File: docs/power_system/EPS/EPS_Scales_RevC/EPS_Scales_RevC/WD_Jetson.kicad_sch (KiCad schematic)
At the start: 40 parts, among them J3 Conn_01x04, J4 Conn_01x04, U5 TLV1704

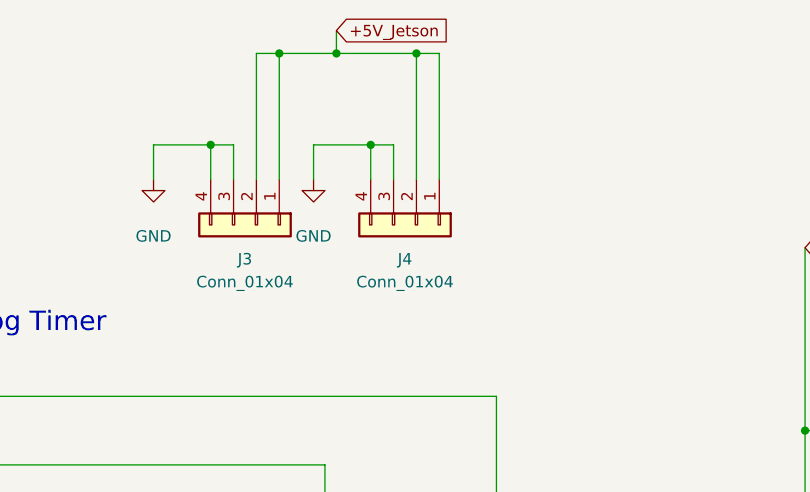
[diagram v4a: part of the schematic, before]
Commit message: WIP EPS REV C.
Removed XNOR implementation, redid layout for compactness, restarting routing for more efficient traces.
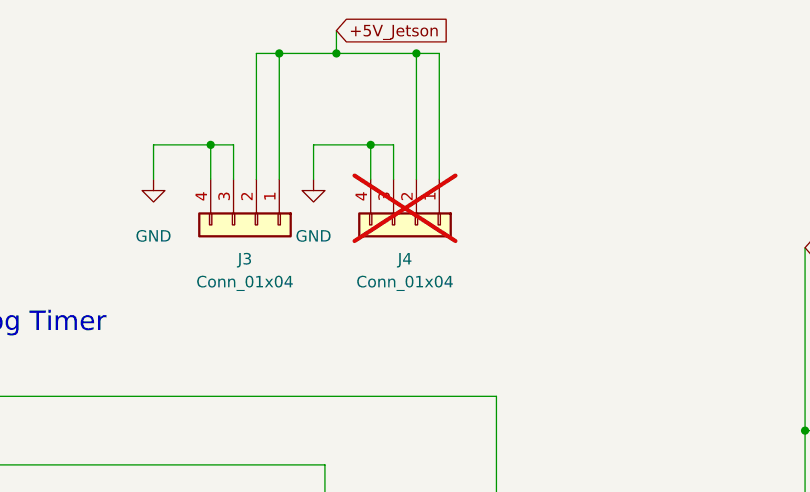
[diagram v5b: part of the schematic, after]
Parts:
- J4: now not fitted
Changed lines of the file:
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@@
 		(exclude_from_sim no)
 		(in_bom yes)
-		(on_board yes)
-		(dnp no)
+		(on_board no)
+		(dnp yes)
 		(fields_autoplaced yes)
 		(property "Reference" "J4"

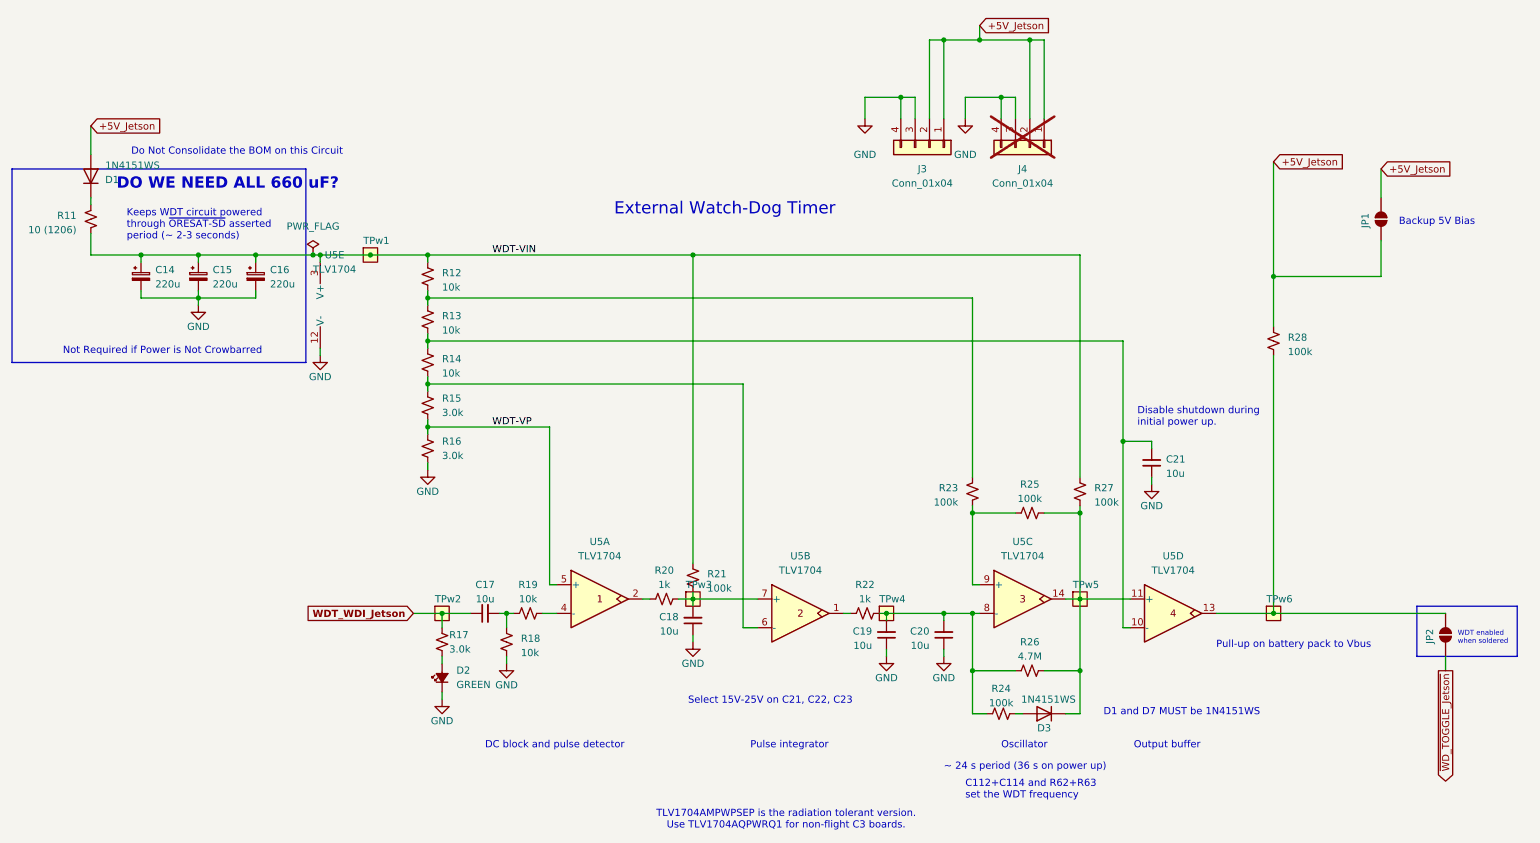
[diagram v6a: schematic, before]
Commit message: Revisions made to schematic include the following
-REV C Dev Board Revision Suggestions from Andrew Greenberg (4/1/25)
               Main Concerns:
               - Stop working on layout so you dont waste your time [DONE]
               - Rename +28V as Vbatt and display voltage ranges (Vbatt = [24.0, 28.8, 33.6]) [DONE]
                  -Reconfigure the UV and OV numbers to allow for this voltage range [DONE]
                     - Modify in the calculations page (be sure to note the numbers)
               - 100nF caps on +28V inputs can be removed due to 10uF [DONE]
               - Ensure the capacitors are +75v rated so they dont explode at the input side [DONE]
                  -Must be ceramic [DONE]
                  -Must be around double of what the peak input voltage is for safe margins [DONE]

               SISB46DN: [DONE]
                  -Replace symbol with 2 MOSFETS so that the end user can understand what the schematic actually represents
               INA230:
                  -Calculate proper resistor values for the INA230 voltage and current detection [DONE] (In rev c calcs last page)
                  -Remove 4.7k resistors on the INA230 side, you want to include them on the host side, be sure to add these notes in the schematic [DONE]

               -Physical Design Revision Notes:
                  -For each component go to its manufacturing page and make note of all the component types that are used for the individual designs, this means that the devices that are used for each are recommended by the manufacturer in the evaluation board.

                  -Replace the footprints for all the inductors to ensure they have the proper current ratings and also have proper spacing for additions to it on the board.

                  Manufacturer recommended components around subsystem comcponents: [DONE]
                     LTC4365:
                           -No hard restrictions on component selection for those that will go around it
 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
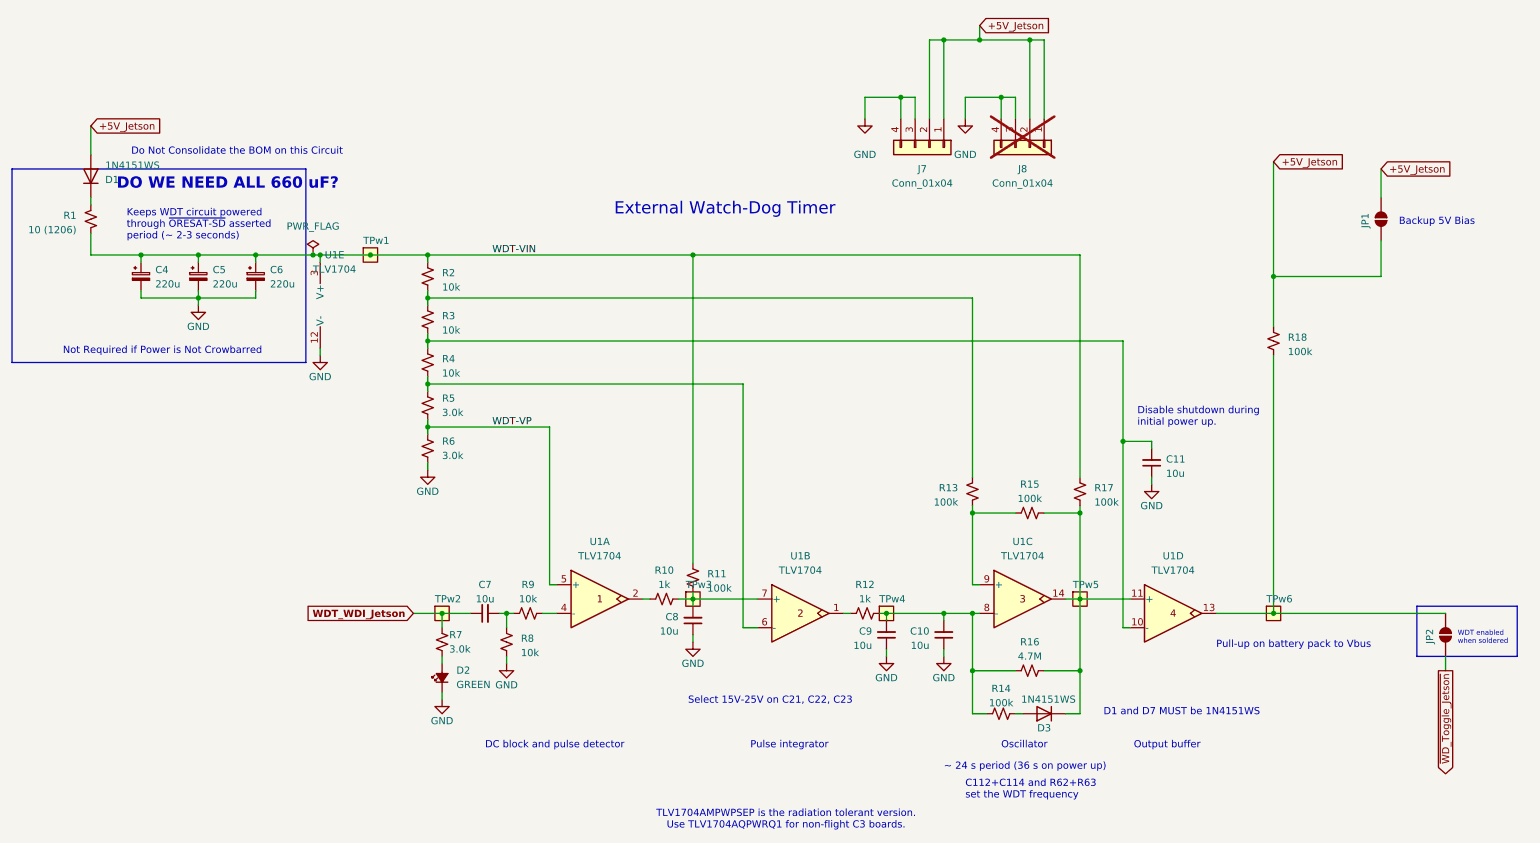
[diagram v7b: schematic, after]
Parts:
- renumbered C20 to C10, C21 to C11, C14 to C4, C15 to C5, C16 to C6, C17 to C7, C18 to C8, C19 to C9, J3 to J7, J4 to J8, R11 to R1, R20 to R10, R21 to R11, R22 to R12, R23 to R13, R24 to R14, R25 to R15, R26 to R16, R27 to R17, R28 to R18, R12 to R2, R13 to R3, R14 to R4, R15 to R5, R16 to R6, R17 to R7, R18 to R8, R19 to R9, U5 to U1
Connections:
- net ~{WD_TOGGLE_Jetson} renamed ~{WD_Toggle_Jetson}

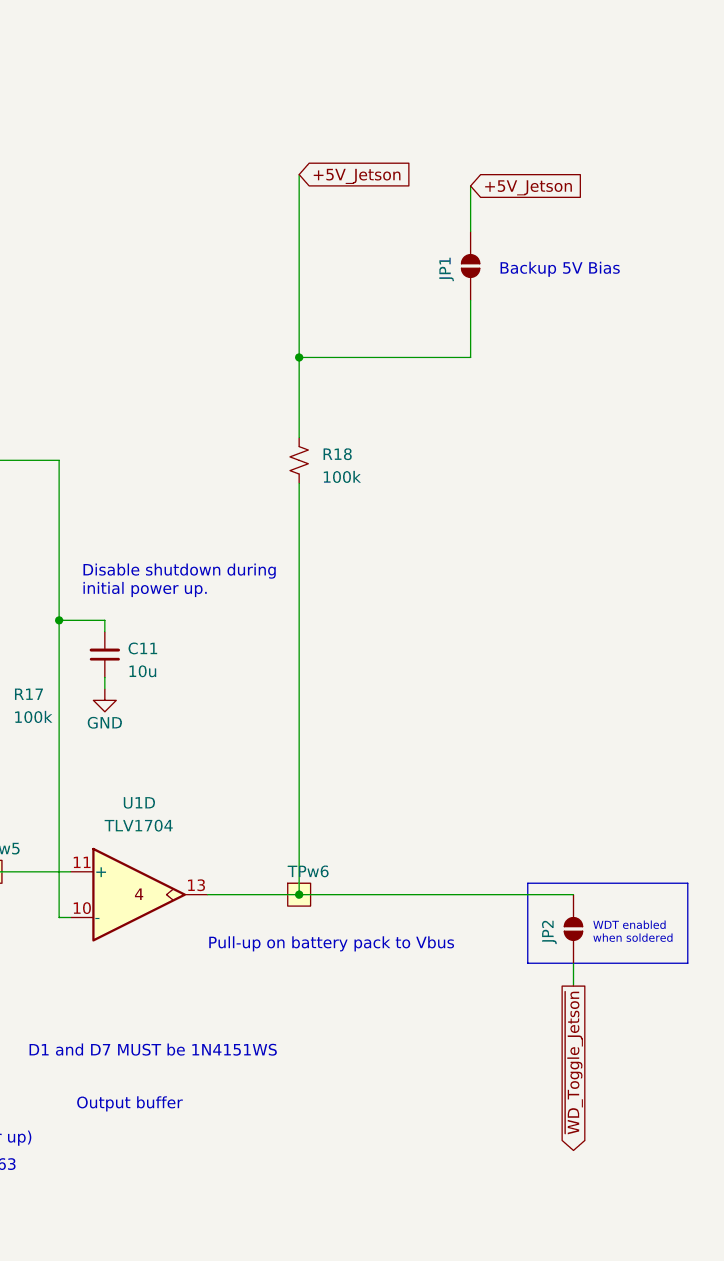
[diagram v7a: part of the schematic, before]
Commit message: Pulled down Perif and Jetson WD
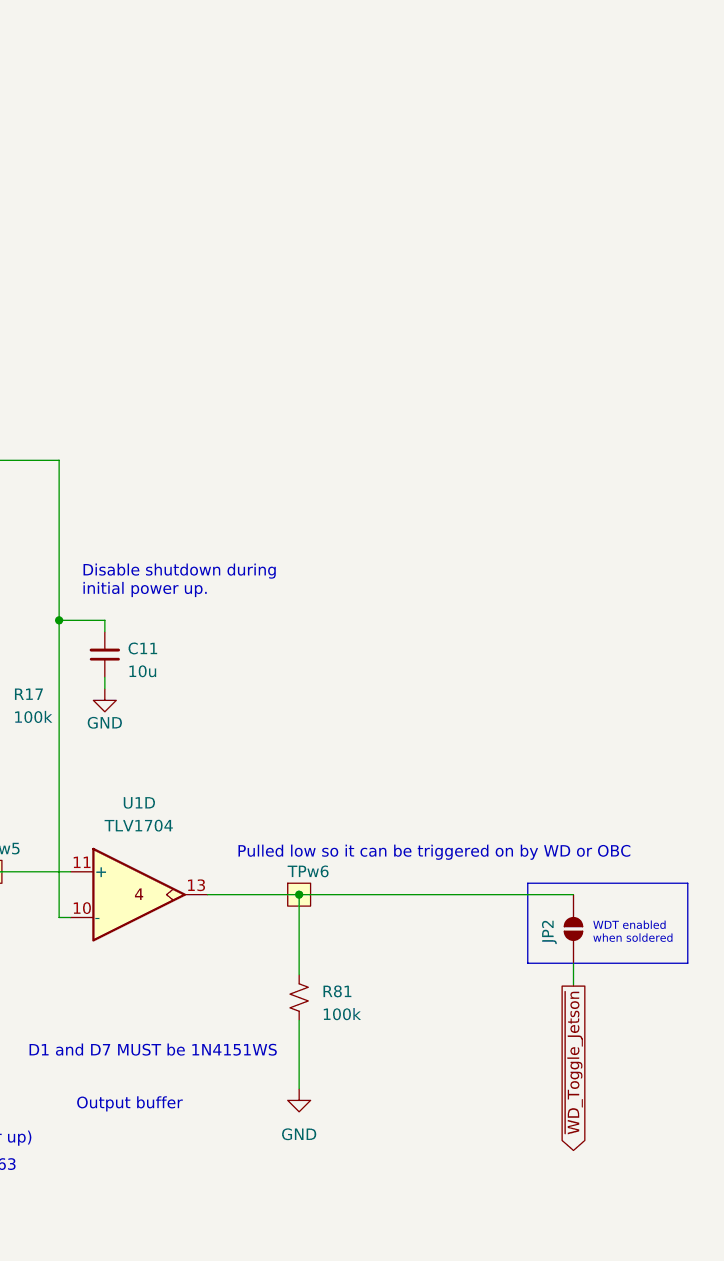
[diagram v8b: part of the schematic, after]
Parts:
- removed JP1: SolderJumper_2_Open, Jumper:SolderJumper-2_P1.3mm_Open_RoundedPad1.0x1.5mm, symbol Jumper:SolderJumper_2_Open
- removed R18: 100k, Resistor_SMD:R_0603_1608Metric, symbol Device:R_Small_US
- added R81: 100k, Resistor_SMD:R_0603_1608Metric, symbol Device:R_Small_US
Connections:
- net GND: now also R81.1
- net at JP2.1 (A), TPw6.1, U1.13: now also R81.2
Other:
- note added: "Pulled low so it can be triggered on by WD or OBC"
- note removed: "Backup 5V Bias"
- note removed: "Pull-up on battery pack to Vbus"
